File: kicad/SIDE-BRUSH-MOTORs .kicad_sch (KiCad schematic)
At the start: 12 parts, among them J15 SIDE BRUSH RIGHT, J16 SIDE BRUSH LEFT, Q16 AO3400, Q18 AO3400

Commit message: Battery charging
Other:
- note added: "Isn't Diode reversed?"
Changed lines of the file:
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@@
 	(generator_version "10.0")
 	(paper "A2")
+	(text "Isn't Diode reversed?"
+		(exclude_from_sim no)
+		(at 254 158.75 0)
+		(effects
+			(font
+				(size 1.27 1.27)
+			)
+		)
+	)
+	(text "Isn't Diode reversed?"
+		(exclude_from_sim no)
+		(at 257.175 249.555 0)
+		(effects
+			(font
+				(size 1.27 1.27)
+			)
+		)
+	)
 	(text "SIDE BRUSH MOTOR CONTROL"
 		(exclude_from_sim no)

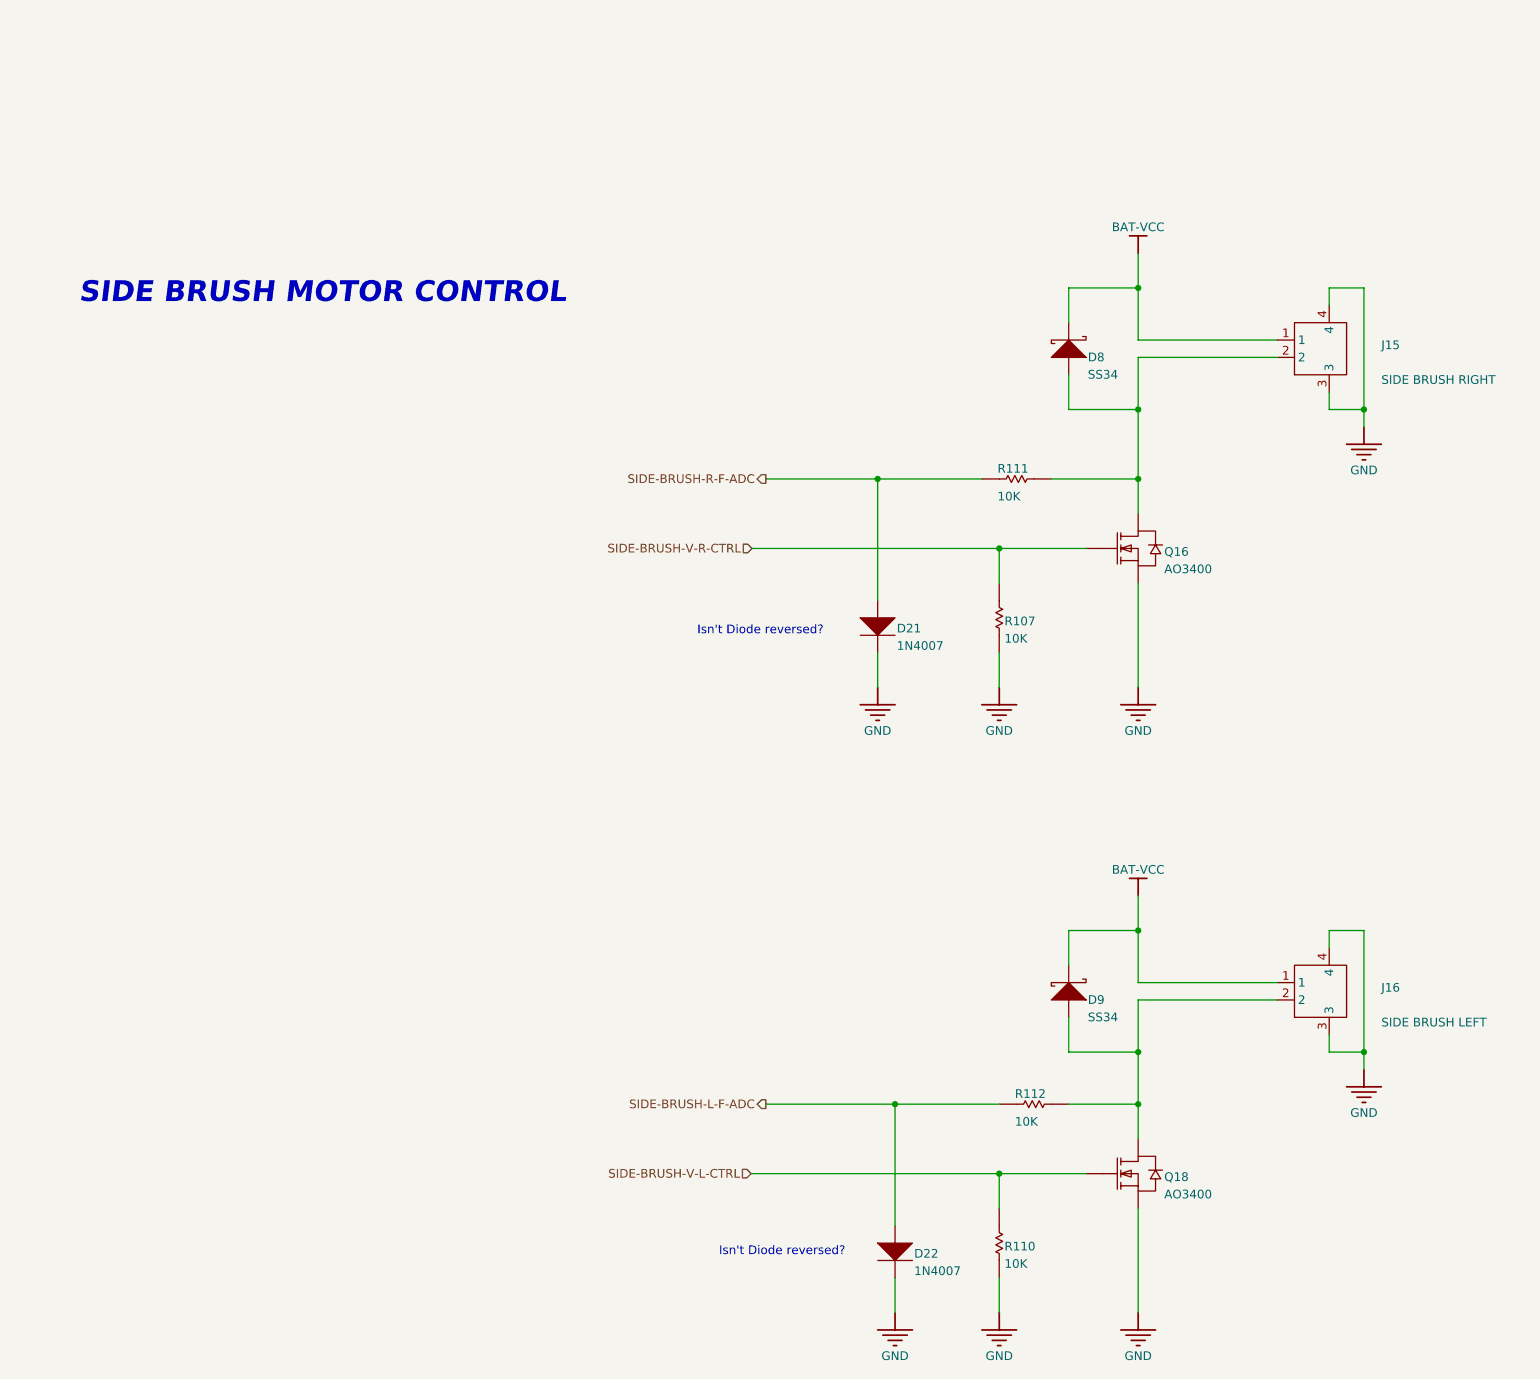
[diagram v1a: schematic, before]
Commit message: Changed MCU to STM32G473VCT6
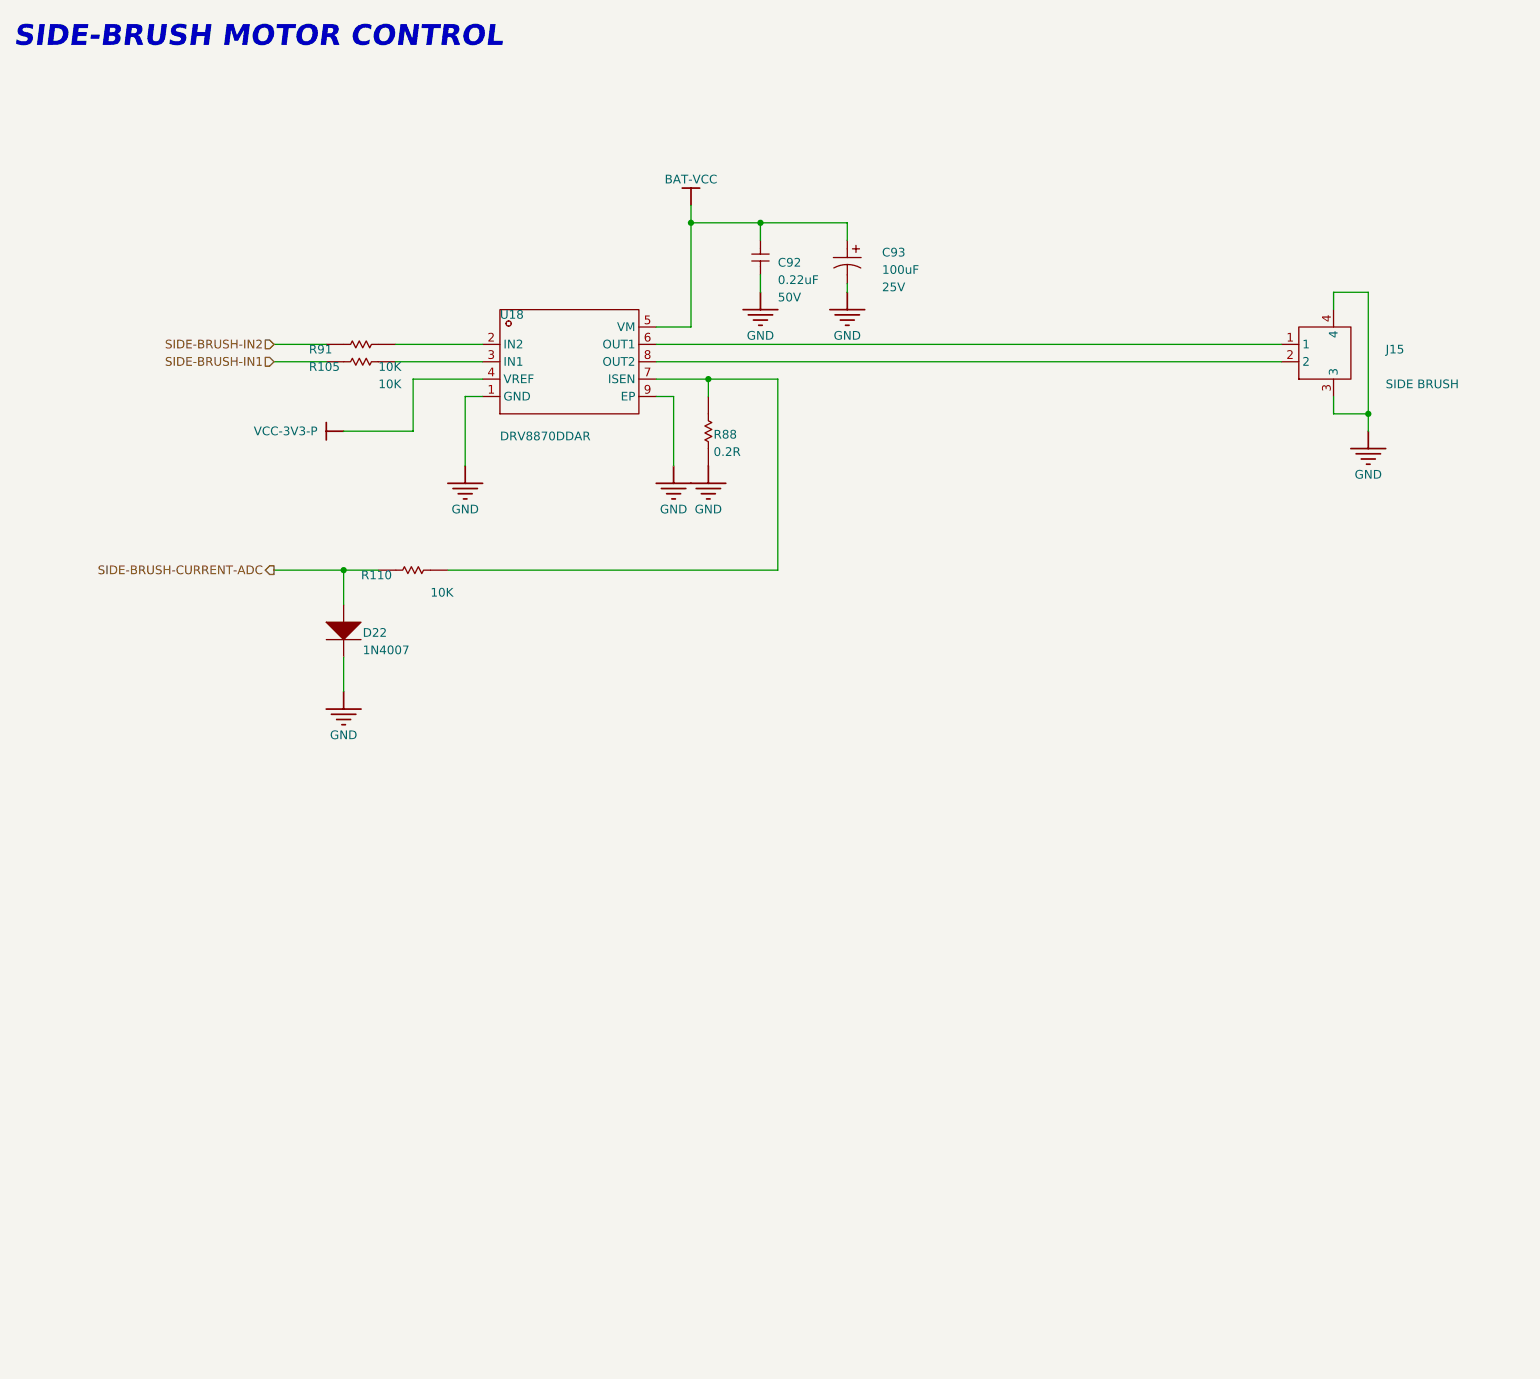
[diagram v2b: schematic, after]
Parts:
- removed D21, D22: 1N4007, oomwoo_altium:SOD123, symbol DesignLibrary:SIDE-BRUSH_3_DIODE-1_DesignLibrary.SchLib
- removed D8, D9: SS34, oomwoo_altium:SMA, symbol DesignLibrary:SIDE-BRUSH_1_DIODE-2_DesignLibrary.SchLib
- removed J16: SIDE BRUSH LEFT, oomwoo_altium:CONN-SMD_2P-P1.50_ZX-ZH1.5-2PWT, symbol DesignLibrary:SIDE-BRUSH_0_HDRx2_DesignLibrary.SchLib
- removed Q16, Q18: AO3400, oomwoo_altium:SOT23-3D, symbol DesignLibrary:SIDE-BRUSH_0_N-MOS-SOT23_DesignLibrary.SchLib
- removed R107, R110: 10K, oomwoo_altium:RES-0402, symbol DesignLibrary:SIDE-BRUSH_1_Resistor-1_DesignLibrary.SchLib
- removed R111, R112: 10K, oomwoo_altium:RES-0402, symbol DesignLibrary:SIDE-BRUSH_2_Resistor-1_DesignLibrary.SchLib
- added C92: 0.22uF, Capacitor_SMD:C_0603_1608Metric, symbol DesignLibrary:WHEEL MOTOR_1_Capacitor-1_DesignLibrary.SchLib
- added C93: 100uF, oomwoo_altium:CAP-SMD_BD6.3-L6.6-W6.6-FD, symbol DesignLibrary:WHEEL MOTOR_3_Capacitor-2_DesignLibrary.SchLib
- added D22: 1N4007, oomwoo_altium:SOD123, symbol DesignLibrary:WHEEL MOTOR_3_DIODE-1_DesignLibrary.SchLib
- added R105, R110, R91: 10K, Resistor_SMD:R_0603_1608Metric, symbol DesignLibrary:WHEEL MOTOR_0_Resistor-1_DesignLibrary.SchLib
- added R88: 0.2R, Resistor_SMD:R_0603_1608Metric, symbol DesignLibrary:WHEEL MOTOR_1_Resistor-1_DesignLibrary.SchLib
- added U18: DRV8870DDAR, oomwoo_altium:HSOP-8_L5.0-W4.0-P1.27-LS6.2-BL-EP, symbol DesignLibrary:WHEEL MOTOR_0_DRV8870_DesignLibrary.SchLib
- J15: value SIDE BRUSH RIGHT -> SIDE BRUSH
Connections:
- net BAT-VCC: now also C92.2, C93.1, U18.5 (VM); no longer J15.1
- net GND: now also C92.1, C93.2, D22.2 (K), R88.1, U18.1 (GND), U18.9 (EP)
- net at J15.2: now also U18.8 (OUT2)
- new net: R91.2, U18.2 (IN2)
- new net: R110.2, R88.2, U18.7 (ISEN)
- new net: R105.2, U18.3 (IN1)
- new net: J15.1, U18.6 (OUT1)
- new net SIDE-BRUSH-CURRENT-ADC: D22.1 (A), R110.1
- new net SIDE-BRUSH-IN1: R105.1
- new net SIDE-BRUSH-IN2: R91.1
- new net VCC-3V3-P: U18.4 (VREF)
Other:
- note added: "SIDE-BRUSH MOTOR CONTROL"
- note removed: "Isn't Diode reversed?"
- note removed: "SIDE BRUSH MOTOR CONTROL"
- moved on the sheet: J15

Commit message: RTC clock, signal integrity
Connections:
- net BAT-VCC renamed VM-VBAT
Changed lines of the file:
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@@
+		)
+	)
+	(global_label "VM-VBAT"
+		(shape input)
+		(at 243.84 96.52 90)
+		(fields_autoplaced yes)
+		(effects
+			(font
+				(size 1.27 1.27)
+			)
+			(justify left)
+		)
+		(property "Intersheetrefs" "${INTERSHEET_REFS}"
+			(at 243.84 85.0076 90)
+			(hide yes)
+			(show_name no)
+			(do_not_autoplace no)
+			(effects
+				(font
+					(size 1.27 1.27)
+				)
+				(justify left)
+			)
 		)
 	)
@@
 					(unit 1)
 				)
-			)
-		)
-	)
-	(symbol
-		(lib_id "oomwoo-kicad-altium-import:BAT-VCC_BAR")
-		(at 243.84 96.52 180)
-		(unit 1)
-		(body_style 1)
-		(exclude_from_sim no)
-		(in_bom yes)
-		(on_board yes)
-		(in_pos_files yes)
-		(dnp no)
-		(property "Reference" "#PWR0587"
-			(at 243.84 96.52 0)
-			(hide yes)
-			(show_name no)
-			(do_not_autoplace no)
-			(effects
-				(font
-					(size 1.27 1.27)
-				)
-			)
-		)
-		(property "Value" "BAT-VCC"
-			(at 243.84 92.71 0)
-			(show_name no)
-			(do_not_autoplace no)
-			(effects
-				(font
-					(size 1.27 1.27)
-				)
-			)
-		)
-		(property "Footprint" ""
-			(at 243.84 96.52 0)
-			(show_name no)
-			(do_not_autoplace no)
-			(effects
-				(font
-					(size 1.27 1.27)
-				)
-			)
-		)
-		(property "Datasheet" ""
-			(at 243.84 96.52 0)
-			(show_name no)
-			(do_not_autoplace no)
-			(effects
-				(font
-					(size 1.27 1.27)
-				)
-			)
-		)
-		(property "Description" ""
-			(at 243.84 96.52 0)
-			(show_name no)
-			(do_not_autoplace no)
-			(effects
-				(font
-					(size 1.27 1.27)
-				)
-			)
-		)
-		(pin ""
-		)
-		(instances
-			(project "oomwoo-kicad"
-				(path "/dbcfb655-8d45-4808-9a74-2a0eb03372e8/92cc07b9-f65d-4f49-9297-7807acee5c86"
-					(reference "#PWR0587")
-					(unit 1)
-				)
